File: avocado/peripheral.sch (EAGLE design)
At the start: 9 parts

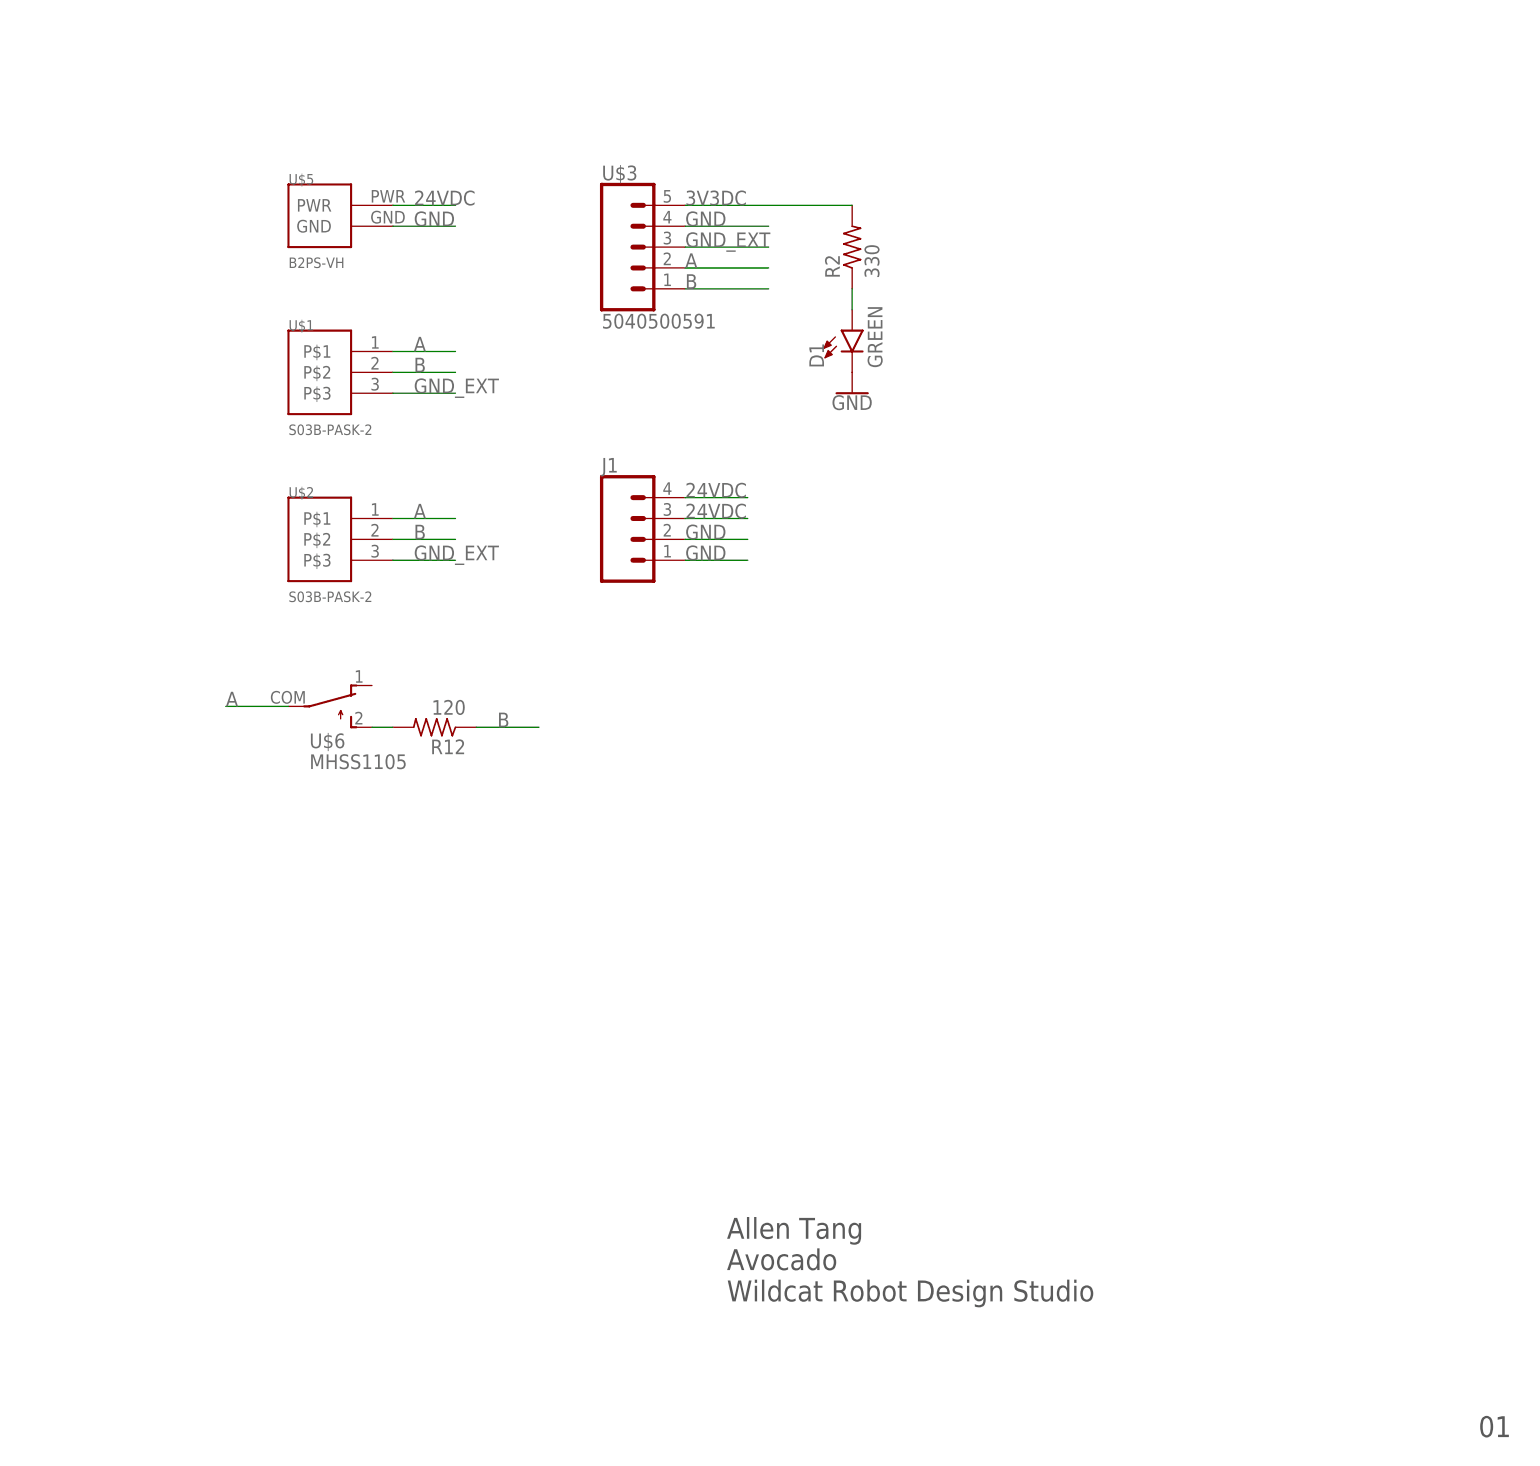
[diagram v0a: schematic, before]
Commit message: updated encoder board size
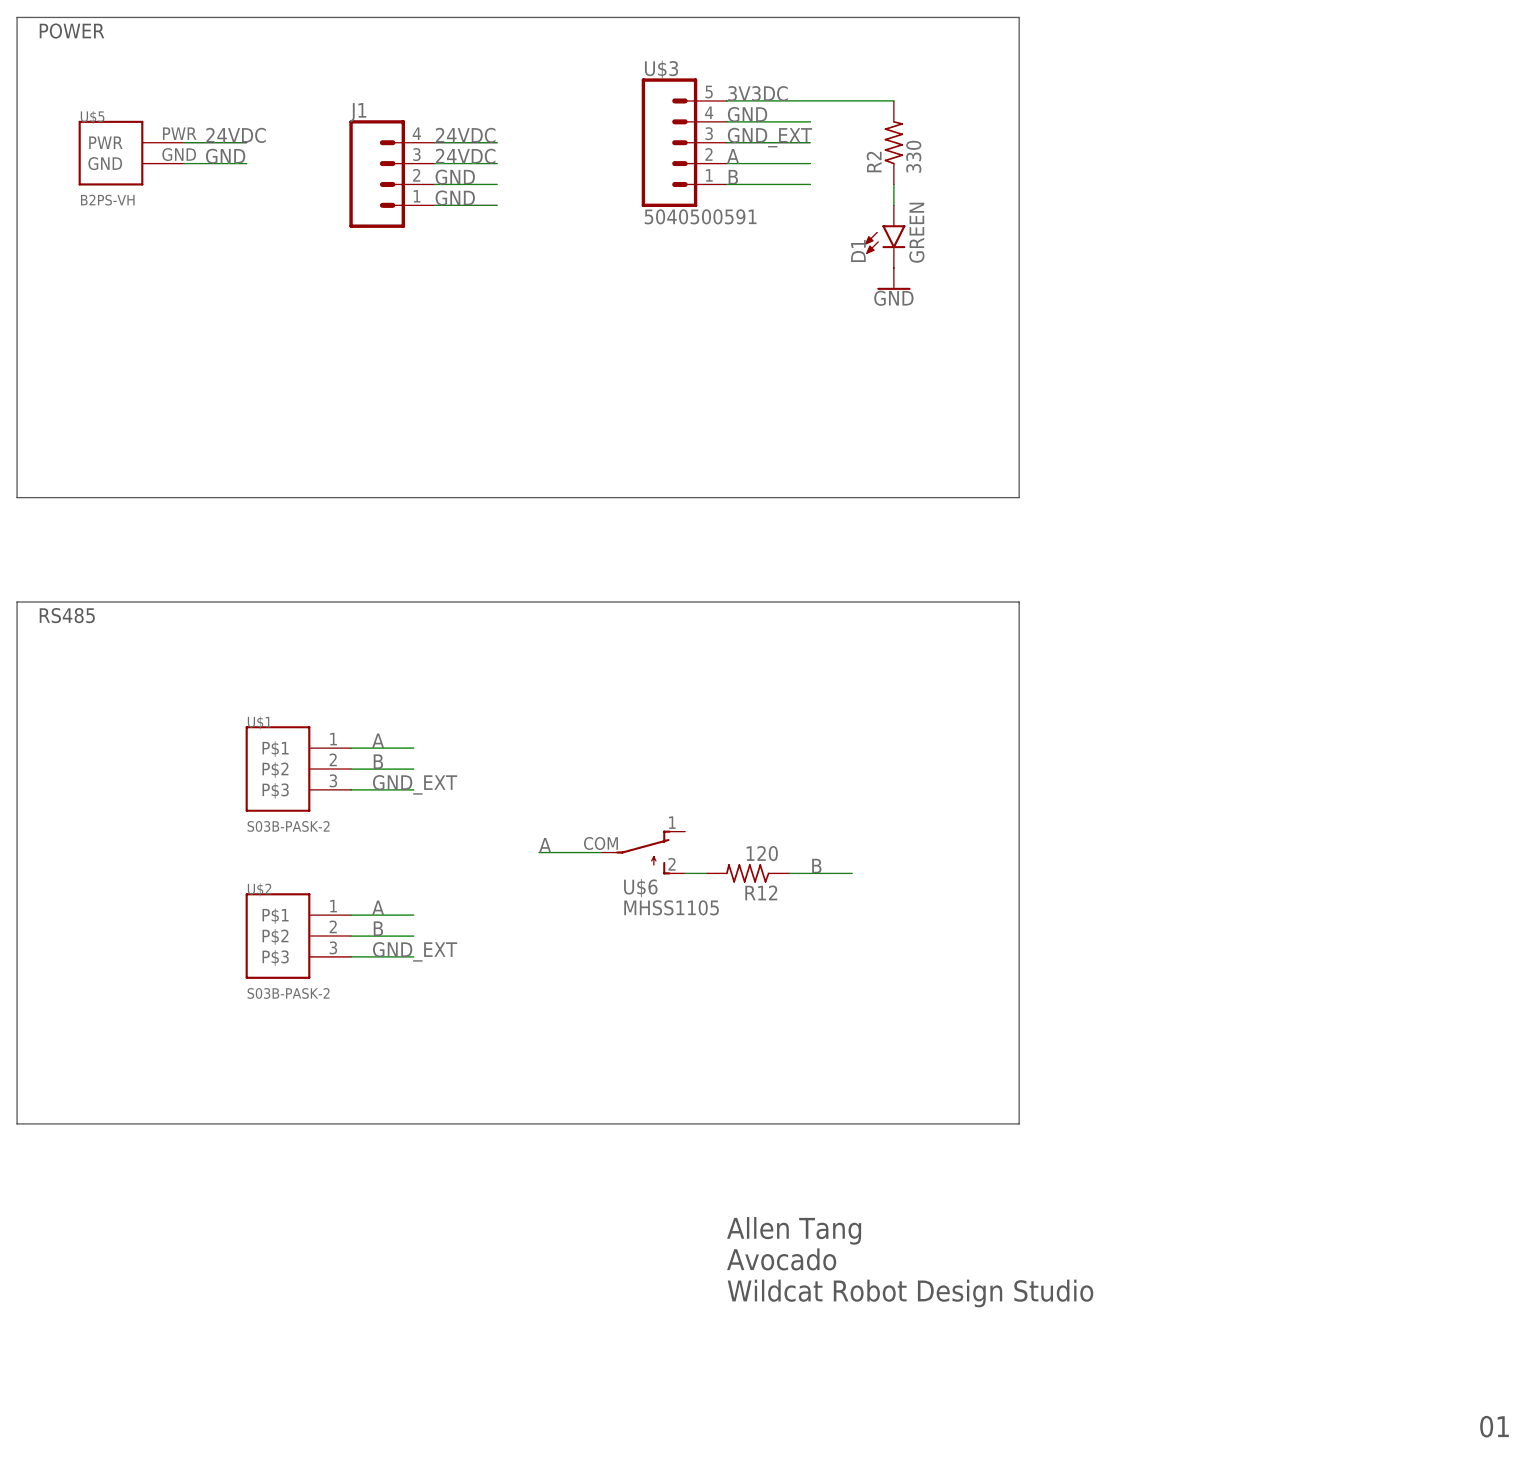
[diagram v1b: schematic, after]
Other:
- note added: "POWER"
- note added: "RS485"
- moved on the sheet: D1, J1, R12, R2, U$1, U$2, U$3, U$5, U$6
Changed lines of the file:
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@@
 Wildcat Robot Design Studio</text>
 <text x="129.54" y="-106.68" size="2.54" layer="97">01</text>
+<wire x1="-48.26" y1="66.04" x2="73.66" y2="66.04" width="0.1524" layer="97"/>
+<wire x1="73.66" y1="66.04" x2="73.66" y2="7.62" width="0.1524" layer="97"/>
+<wire x1="73.66" y1="7.62" x2="-48.26" y2="7.62" width="0.1524" layer="97"/>
+<wire x1="-48.26" y1="7.62" x2="-48.26" y2="66.04" width="0.1524" layer="97"/>
+<wire x1="-48.26" y1="-5.08" x2="73.66" y2="-5.08" width="0.1524" layer="97"/>
+<wire x1="73.66" y1="-5.08" x2="73.66" y2="-68.58" width="0.1524" layer="97"/>
+<wire x1="73.66" y1="-68.58" x2="-48.26" y2="-68.58" width="0.1524" layer="97"/>
+<wire x1="-48.26" y1="-68.58" x2="-48.26" y2="-5.08" width="0.1524" layer="97"/>
+<text x="-45.72" y="63.5" size="1.778" layer="97">POWER</text>
+<text x="-45.72" y="-7.62" size="1.778" layer="97">RS485</text>
 </plain>
 <instances>
-<instance part="U$1" gate="G$1" x="-12.7" y="22.86"/>
-<instance part="U$2" gate="G$1" x="-12.7" y="2.54"/>
-<instance part="U$5" gate="G$1" x="-10.16" y="40.64"/>
-<instance part="U$6" gate="G$1" x="-10.16" y="-17.78" rot="R270"/>
-<instance part="R12" gate="G$1" x="2.54" y="-20.32" rot="R180"/>
+<instance part="U$1" gate="G$1" x="-17.78" y="-25.4"/>
+<instance part="U$2" gate="G$1" x="-17.78" y="-45.72"/>
+<instance part="U$5" gate="G$1" x="-35.56" y="48.26"/>
+<instance part="U$6" gate="G$1" x="27.94" y="-35.56" rot="R270"/>
+<instance part="R12" gate="G$1" x="40.64" y="-38.1" rot="R180"/>
 <instance part="FRAME1" gate="G$1" x="-137.16" y="-114.3"/>
 <instance part="FRAME1" gate="G$2" x="35.56" y="-114.3"/>
-<instance part="D1" gate="G$1" x="53.34" y="27.94"/>
-<instance part="GND1" gate="1" x="53.34" y="20.32"/>
-<instance part="J1" gate="G$1" x="27.94" y="2.54"/>
-<instance part="R2" gate="G$1" x="53.34" y="38.1" rot="R90"/>
-<instance part="U$3" gate="G$1" x="25.4" y="38.1"/>
+<instance part="D1" gate="G$1" x="58.42" y="40.64"/>
+<instance part="GND1" gate="1" x="58.42" y="33.02"/>
+<instance part="J1" gate="G$1" x="-2.54" y="45.72"/>
+<instance part="R2" gate="G$1" x="58.42" y="50.8" rot="R90"/>
+<instance part="U$3" gate="G$1" x="30.48" y="50.8"/>
 </instances>
 <busses>
@@
 <segment>
 <pinref part="U$5" gate="G$1" pin="PWR"/>
-<wire x1="-2.54" y1="43.18" x2="5.08" y2="43.18" width="0.1524" layer="91"/>
-<label x="0" y="43.18" size="1.778" layer="95"/>
+<wire x1="-27.94" y1="50.8" x2="-20.32" y2="50.8" width="0.1524" layer="91"/>
+<label x="-25.4" y="50.8" size="1.778" layer="95"/>
 </segment>
 <segment>
 <pinref part="J1" gate="G$1" pin="4"/>
-<wire x1="33.02" y1="7.62" x2="40.64" y2="7.62" width="0.1524" layer="91"/>
-<label x="33.02" y="7.62" size="1.778" layer="95"/>
+<wire x1="2.54" y1="50.8" x2="10.16" y2="50.8" width="0.1524" layer="91"/>
+<label x="2.54" y="50.8" size="1.778" layer="95"/>
 </segment>
 <segment>
 <pinref part="J1" gate="G$1" pin="3"/>
-<wire x1="33.02" y1="5.08" x2="40.64" y2="5.08" width="0.1524" layer="91"/>
-<label x="33.02" y="5.08" size="1.778" layer="95"/>
+<wire x1="2.54" y1="48.26" x2="10.16" y2="48.26" width="0.1524" layer="91"/>
+<label x="2.54" y="48.26" size="1.778" layer="95"/>
 </segment>
 </net>
@@
 <segment>
 <pinref part="U$3" gate="G$1" pin="4"/>
-<wire x1="33.02" y1="40.64" x2="43.18" y2="40.64" width="0.1524" layer="91"/>
-<label x="33.02" y="40.64" size="1.778" layer="95"/>
+<wire x1="38.1" y1="53.34" x2="48.26" y2="53.34" width="0.1524" layer="91"/>
+<label x="38.1" y="53.34" size="1.778" layer="95"/>
 </segment>
 <segment>
 <pinref part="J1" gate="G$1" pin="2"/>
-<wire x1="33.02" y1="2.54" x2="40.64" y2="2.54" width="0.1524" layer="91"/>
-<label x="33.02" y="2.54" size="1.778" layer="95"/>
+<wire x1="2.54" y1="45.72" x2="10.16" y2="45.72" width="0.1524" layer="91"/>
+<label x="2.54" y="45.72" size="1.778" layer="95"/>
 </segment>
 <segment>
 <pinref part="J1" gate="G$1" pin="1"/>
-<wire x1="33.02" y1="0" x2="40.64" y2="0" width="0.1524" layer="91"/>
-<label x="33.02" y="0" size="1.778" layer="95"/>
+<wire x1="2.54" y1="43.18" x2="10.16" y2="43.18" width="0.1524" layer="91"/>
+<label x="2.54" y="43.18" size="1.778" layer="95"/>
 </segment>
 <segment>
 <pinref part="U$5" gate="G$1" pin="GND"/>
-<wire x1="-2.54" y1="40.64" x2="5.08" y2="40.64" width="0.1524" layer="91"/>
-<label x="0" y="40.64" size="1.778" layer="95"/>
+<wire x1="-27.94" y1="48.26" x2="-20.32" y2="48.26" width="0.1524" layer="91"/>
+<label x="-25.4" y="48.26" size="1.778" layer="95"/>
 </segment>
 </net>
@@
 <segment>
 <pinref part="U$1" gate="G$1" pin="P$3"/>
-<wire x1="-2.54" y1="20.32" x2="5.08" y2="20.32" width="0.1524" layer="91"/>
-<label x="0" y="20.32" size="1.778" layer="95"/>
+<wire x1="-7.62" y1="-27.94" x2="0" y2="-27.94" width="0.1524" layer="91"/>
+<label x="-5.08" y="-27.94" size="1.778" layer="95"/>
 </segment>
 <segment>
 <pinref part="U$2" gate="G$1" pin="P$3"/>
-<wire x1="-2.54" y1="0" x2="5.08" y2="0" width="0.1524" layer="91"/>
-<label x="0" y="0" size="1.778" layer="95"/>
+<wire x1="-7.62" y1="-48.26" x2="0" y2="-48.26" width="0.1524" layer="91"/>
+<label x="-5.08" y="-48.26" size="1.778" layer="95"/>
 </segment>
 <segment>
 <pinref part="U$3" gate="G$1" pin="3"/>
-<wire x1="33.02" y1="38.1" x2="43.18" y2="38.1" width="0.1524" layer="91"/>
-<label x="33.02" y="38.1" size="1.778" layer="95"/>
+<wire x1="38.1" y1="50.8" x2="48.26" y2="50.8" width="0.1524" layer="91"/>
+<label x="38.1" y="50.8" size="1.778" layer="95"/>
 </segment>
 </net>
@@
 <segment>
 <pinref part="U$1" gate="G$1" pin="P$2"/>
-<wire x1="-2.54" y1="22.86" x2="5.08" y2="22.86" width="0.1524" layer="91"/>
-<label x="0" y="22.86" size="1.778" layer="95"/>
+<wire x1="-7.62" y1="-25.4" x2="0" y2="-25.4" width="0.1524" layer="91"/>
+<label x="-5.08" y="-25.4" size="1.778" layer="95"/>
 </segment>
 <segment>
 <pinref part="U$2" gate="G$1" pin="P$2"/>
-<wire x1="-2.54" y1="2.54" x2="5.08" y2="2.54" width="0.1524" layer="91"/>
-<label x="0" y="2.54" size="1.778" layer="95"/>
+<wire x1="-7.62" y1="-45.72" x2="0" y2="-45.72" width="0.1524" layer="91"/>
+<label x="-5.08" y="-45.72" size="1.778" layer="95"/>
 </segment>
 <segment>
 <pinref part="R12" gate="G$1" pin="1"/>
-<wire x1="7.62" y1="-20.32" x2="15.24" y2="-20.32" width="0.1524" layer="91"/>
-<label x="10.16" y="-20.32" size="1.778" layer="95"/>
+<wire x1="45.72" y1="-38.1" x2="53.34" y2="-38.1" width="0.1524" layer="91"/>
+<label x="48.26" y="-38.1" size="1.778" layer="95"/>
 </segment>
 <segment>
 <pinref part="U$3" gate="G$1" pin="1"/>
-<wire x1="33.02" y1="33.02" x2="43.18" y2="33.02" width="0.1524" layer="91"/>
-<label x="33.02" y="33.02" size="1.778" layer="95"/>
+<wire x1="38.1" y1="45.72" x2="48.26" y2="45.72" width="0.1524" layer="91"/>
+<label x="38.1" y="45.72" size="1.778" layer="95"/>
 </segment>
 </net>
@@
 <segment>
 <pinref part="U$1" gate="G$1" pin="P$1"/>
-<wire x1="-2.54" y1="25.4" x2="5.08" y2="25.4" width="0.1524" layer="91"/>
-<label x="0" y="25.4" size="1.778" layer="95"/>
+<wire x1="-7.62" y1="-22.86" x2="0" y2="-22.86" width="0.1524" layer="91"/>
+<label x="-5.08" y="-22.86" size="1.778" layer="95"/>
 </segment>
 <segment>
 <pinref part="U$2" gate="G$1" pin="P$1"/>
-<wire x1="-2.54" y1="5.08" x2="5.08" y2="5.08" width="0.1524" layer="91"/>
-<label x="0" y="5.08" size="1.778" layer="95"/>
+<wire x1="-7.62" y1="-43.18" x2="0" y2="-43.18" width="0.1524" layer="91"/>
+<label x="-5.08" y="-43.18" size="1.778" layer="95"/>
 </segment>
 <segment>
 <pinref part="U$6" gate="G$1" pin="COM"/>
-<wire x1="-15.24" y1="-17.78" x2="-22.86" y2="-17.78" width="0.1524" layer="91"/>
-<label x="-22.86" y="-17.78" size="1.778" layer="95"/>
+<wire x1="22.86" y1="-35.56" x2="15.24" y2="-35.56" width="0.1524" layer="91"/>
+<label x="15.24" y="-35.56" size="1.778" layer="95"/>
 </segment>
 <segment>
 <pinref part="U$3" gate="G$1" pin="2"/>
-<wire x1="33.02" y1="35.56" x2="43.18" y2="35.56" width="0.1524" layer="91"/>
-<label x="33.02" y="35.56" size="1.778" layer="95"/>
+<wire x1="38.1" y1="48.26" x2="48.26" y2="48.26" width="0.1524" layer="91"/>
+<label x="38.1" y="48.26" size="1.778" layer="95"/>
 </segment>
 </net>
@@
 <pinref part="U$6" gate="G$1" pin="2"/>
 <pinref part="R12" gate="G$1" pin="2"/>
-<wire x1="-2.54" y1="-20.32" x2="-5.08" y2="-20.32" width="0.1524" layer="91"/>
+<wire x1="35.56" y1="-38.1" x2="33.02" y2="-38.1" width="0.1524" layer="91"/>
 </segment>
 </net>
@@
 <segment>
 <pinref part="U$3" gate="G$1" pin="5"/>
-<wire x1="33.02" y1="43.18" x2="53.34" y2="43.18" width="0.1524" layer="91"/>
-<label x="33.02" y="43.18" size="1.778" layer="95"/>
+<wire x1="38.1" y1="55.88" x2="58.42" y2="55.88" width="0.1524" layer="91"/>
+<label x="38.1" y="55.88" size="1.778" layer="95"/>
 <pinref part="R2" gate="G$1" pin="2"/>
 </segment>
@@
 <pinref part="D1" gate="G$1" pin="A"/>
 <pinref part="R2" gate="G$1" pin="1"/>
-<wire x1="53.34" y1="33.02" x2="53.34" y2="30.48" width="0.1524" layer="91"/>
+<wire x1="58.42" y1="45.72" x2="58.42" y2="43.18" width="0.1524" layer="91"/>
 </segment>
 </net>
